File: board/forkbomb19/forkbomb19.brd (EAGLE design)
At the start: 89.2 x 57 mm, 55 parts, among them SW1 SPST_TACT-KMR2, U1 ESP-WROOM-03, X3 POT_GND, X4 POT_3V3, X5 POT_SIG

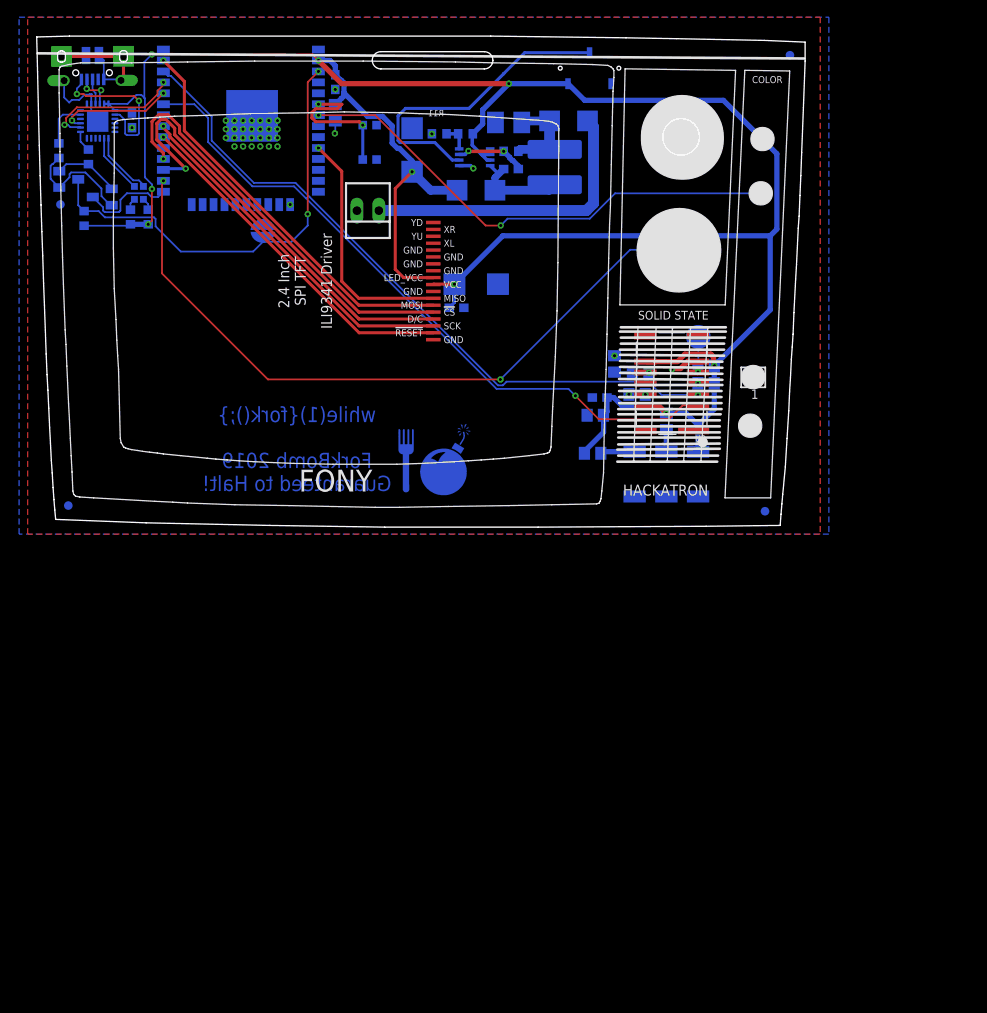
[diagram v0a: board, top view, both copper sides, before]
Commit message: moving to lithium batteries
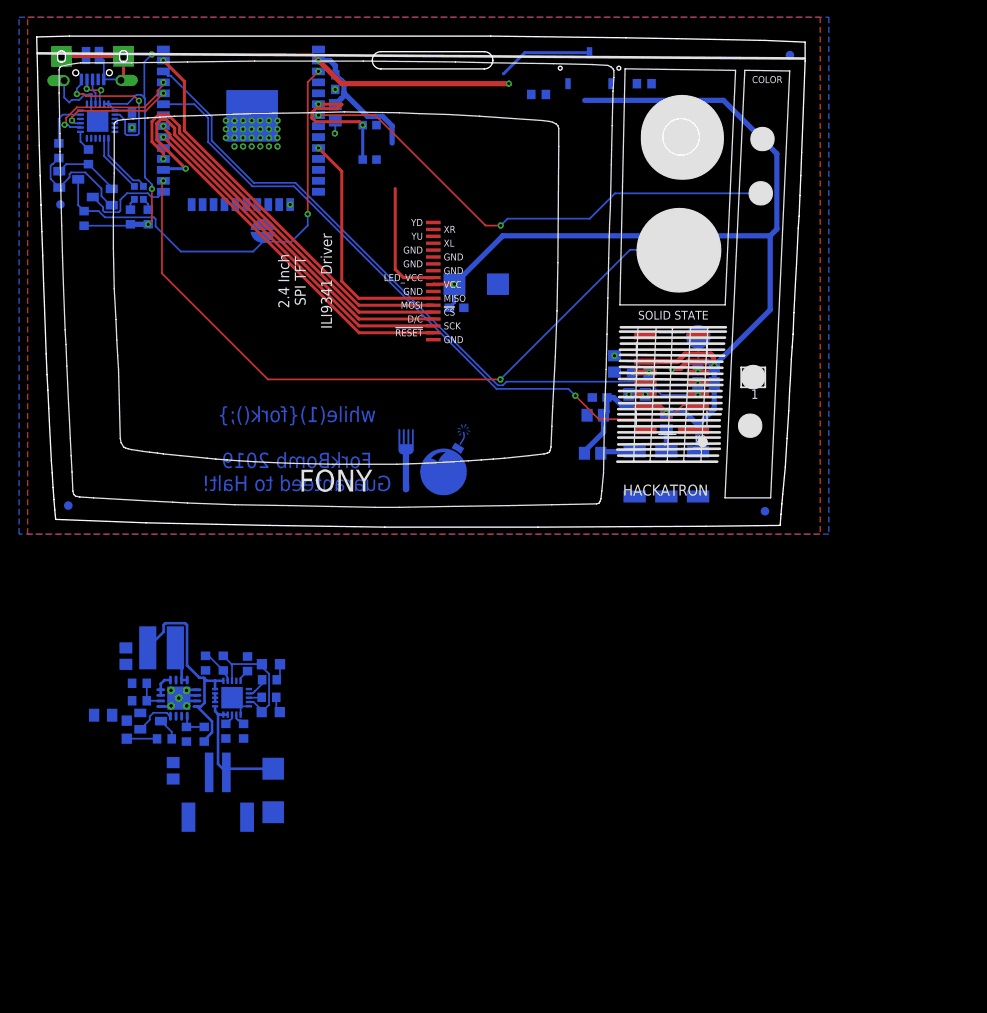
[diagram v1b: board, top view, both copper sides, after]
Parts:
- removed BATT: 22-23-2021, con-molex:22-23-2021
- removed C11: 4.7pF, resistor:C0603
- removed C12: 100uF, resistor:C/6032-28R
- removed D1, D2: MBRS130LT3, diode:SMB
- removed L1: 4.7uH, resistor:POWER-CHOKE_WE-TPC
- removed R10: 165k, resistor:R0603
- removed R11: 100k, resistor:R0603
- removed U$1: LM2623, forkbomb19:SSOP08
- added B1: JST 2-PH, microbuilder:JSTPH2
- added C15: 2.2uF, rcl:C0805
- added C16: 0.1uF, microbuilder:0805_10MGAP
- added C2: 10uF, microbuilder:0805-NO
- added CHRG/LBO: ORANGE, microbuilder:CHIPLED_0805_NOOUTLINE
- added DONE: GREEN, microbuilder:CHIPLED_0805_NOOUTLINE
- added L2: 6.8uH, microbuilder:INDUCTOR_5X5MM_TDK_VLC5045
- added LED1: RED, microbuilder:CHIPLED_0805_NOOUTLINE
- added R18, R21: 200K, rcl:R0603
- added R19: 1.12M, rcl:R0603
- added R20, R27, R28: 1K, rcl:R0603
- added R23: 340K, rcl:R0603
- added R24: 1.87M, rcl:R0603
- added R25: 270K, rcl:R0603
- added R26, R30: 100K, rcl:R0603
- added R29: 1.0K, rcl:R0603
- added T3: MMUN2133LT1G, transistor:SC59-BEC
- added THERM: 15K, rcl:R0603
- added U4: TPS61090RSAR, microbuilder:PVQFN-16
- added U5: MCP73871, microbuilder:QFN20_4MM
- C10: value 22uF -> 100uF; device resistor:T/3528-12R -> rcl:C/6032-28R
- R9: value 150k -> 200k; device resistor:R0603 -> rcl:R0603
- moved C10 82.2 mm to (26.5, -30.8), turned to 90 degrees
- moved R9 17.3 mm to (69.6, 51.3)
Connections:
- removed net N$14: C11.2, R9.1, U$1.3
- removed net N$15: C11.1, D2.A, L1.2, U$1.8
- removed net N$17: U$1.2, U$17.P$2
- removed net N$18: R10.1, R11.2, U$1.4
- removed net N$30: BATT.1, D1.A
- new net ENABLE: U$17.P$2, U4.11
- new net LBO: T3.B, U4.12
- new net N$16: L2.P$2, U4.3, U4.4
- new net N$23: R23.2, R24.1, U4.9
- new net N$24: LED1.A, R20.1
- new net N$25: R19.1, R21.2, U4.14
- new net N$26: R20.2, T3.C
- new net N$28: R25.1, R26.1, U5.P$2
- new net N$29: R28.1, U5.P$7
- new net N$32: R27.1, U5.P$8
- new net N$33: R29.2, U5.P$13
- new net N$34: THERM.2, U5.P$5
- new net N$35: DONE.C, R28.2
- new net N$36: CHRG/LBO.C, R27.2
- new net N$37: R30.2, U5.P$12
- new net N$42: R18.2, U$17.P$3
- new net VBAT: C16.1, C2.1, L2.P$1, R18.1, R24.2, T3.E, U4.8, U5.P$1, U5.P$20
- new net VBUS: CHRG/LBO.A, DONE.A, R25.2, U5.P$17, U5.P$18, U5.P$19, U5.P$3, U5.P$4, U5.P$9
- new net VLIPO: B1.2, C10.+, U5.P$14, U5.P$15, U5.P$16
- net +3V3: now also C15.1, R19.2, U4.1, U4.15, U4.16; no longer C12.+, D2.C, R10.2, U$1.6, U$1.7, U$17.P$3
- net GND: now also B1.1, C15.2, C16.2, C2.2, LED1.C, R21.1, R23.1, R26.2, R29.1, R30.1, R9.2, THERM.1, U4.10, U4.13, U4.5, U4.6, U4.7, U4.P$18, U4.P$19, U4.P$20, U4.P$21, U4.P$22, U4.THERMAL, U5.P$10, U5.P$11, U5.P$21; no longer BATT.2, C12.-, R11.1, U$1.1, U$1.5, U$17.P$1
- net N$13: now also R9.1, U$17.P$1; no longer C10.+, D1.C, L1.1, R9.2
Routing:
- net N$17: track 36.2 -> 0.00 mm
- net N$30: track 35.1 -> 0.00 mm
- net +3V3: track 286.0 -> 252.9 mm, vias 9 -> 8
- net VBAT: track 0.00 -> 26.0 mm
- net VBUS: track 0.00 -> 16.2 mm
- net N$13: track 15.1 -> 0.00 mm
- net VLIPO: track 0.00 -> 15.1 mm
- net N$15: track 12.9 -> 0.00 mm
- net GND: track 31.7 -> 42.7 mm, vias 36 -> 34
- net ENABLE: track 0.00 -> 11.0 mm
- net N$14: track 8.15 -> 0.00 mm, vias 2 -> 0
- net LBO: track 0.00 -> 4.80 mm
- net N$16: track 0.00 -> 4.70 mm
- net N$28: track 0.00 -> 4.17 mm
- net N$25: track 0.00 -> 3.66 mm
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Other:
- board text removed: "+"
- board text removed: "-"

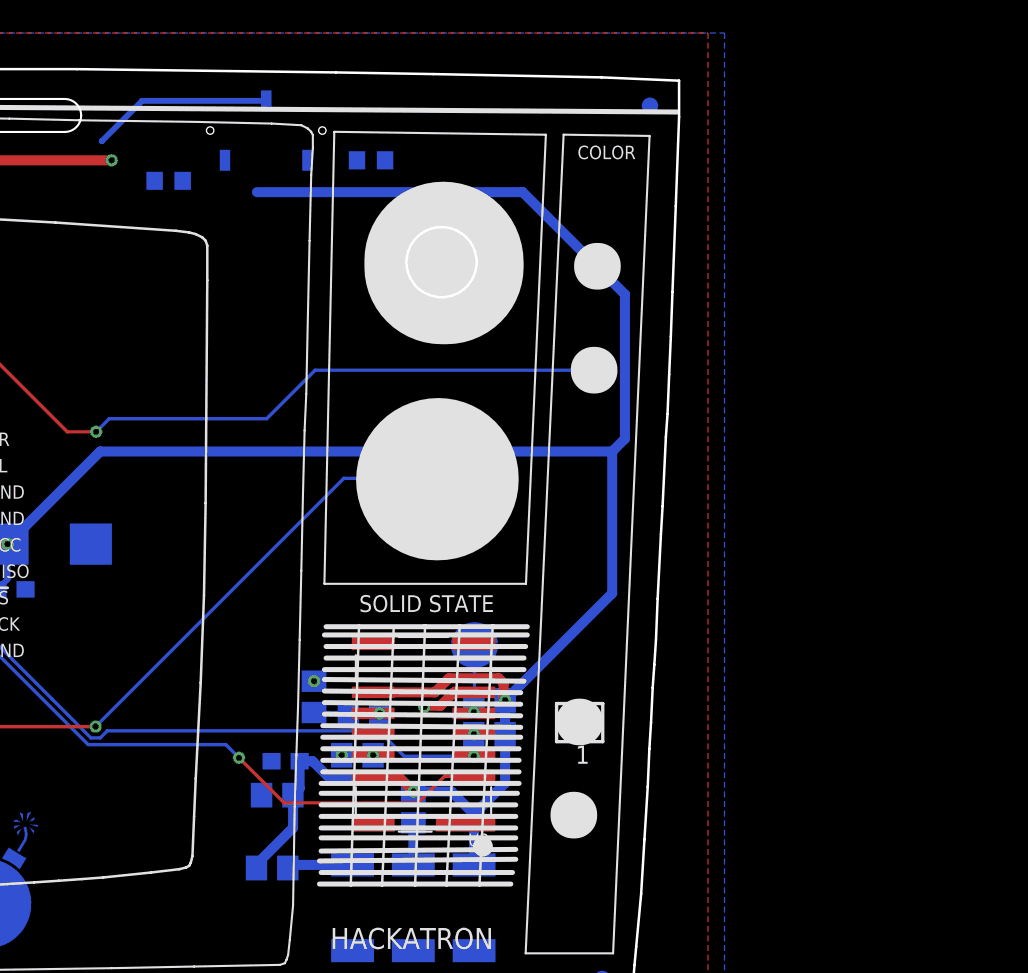
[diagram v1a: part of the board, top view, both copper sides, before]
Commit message: added new thermal sensor part
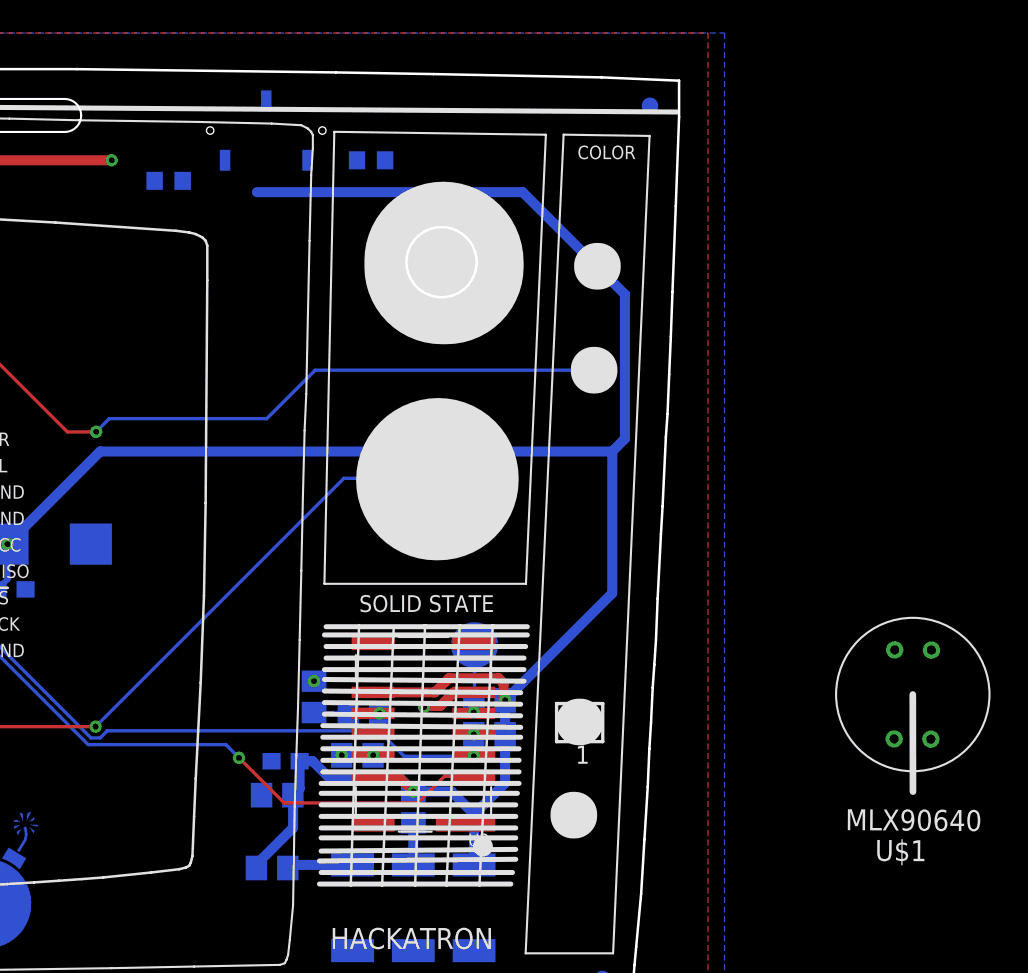
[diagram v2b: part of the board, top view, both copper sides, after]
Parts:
- added U$7: MLX90640, forkbomb19:MLX90640
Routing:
- net ENABLE: track 11.0 -> 0.00 mm
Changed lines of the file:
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@@
 <attribute name="VALUE" x="23.4422" y="-33.7594" size="1.27" layer="28" rot="MR90"/>
 </element>
+<element name="U$7" library="forkbomb19" package="MLX90640" value="MLX90640" x="102.4128" y="18.8976" smashed="yes" rot="R67.2"/>
 </elements>
 <signals>
@@
 <signal name="ENABLE">
 <contactref element="U$17" pad="P$2"/>
-<wire x1="55.6934" y1="54.886" x2="53.2573" y2="52.4499" width="0.3556" layer="16"/>
-<wire x1="53.2573" y1="52.4499" x2="53.2573" y2="52.4420125" width="0.3556" layer="16"/>
-<wire x1="63.2206" y1="54.886" x2="55.6934" y2="54.886" width="0.3556" layer="16"/>
-<wire x1="15.2198" y1="-22.1406" x2="53.2573" y2="52.4499" width="0" layer="19" extent="16-16"/>
 <contactref element="U4" pad="11"/>
+<wire x1="15.2198" y1="-22.1406" x2="63.2206" y2="54.886" width="0" layer="19" extent="16-16"/>
 </signal>
 <signal name="N$25">

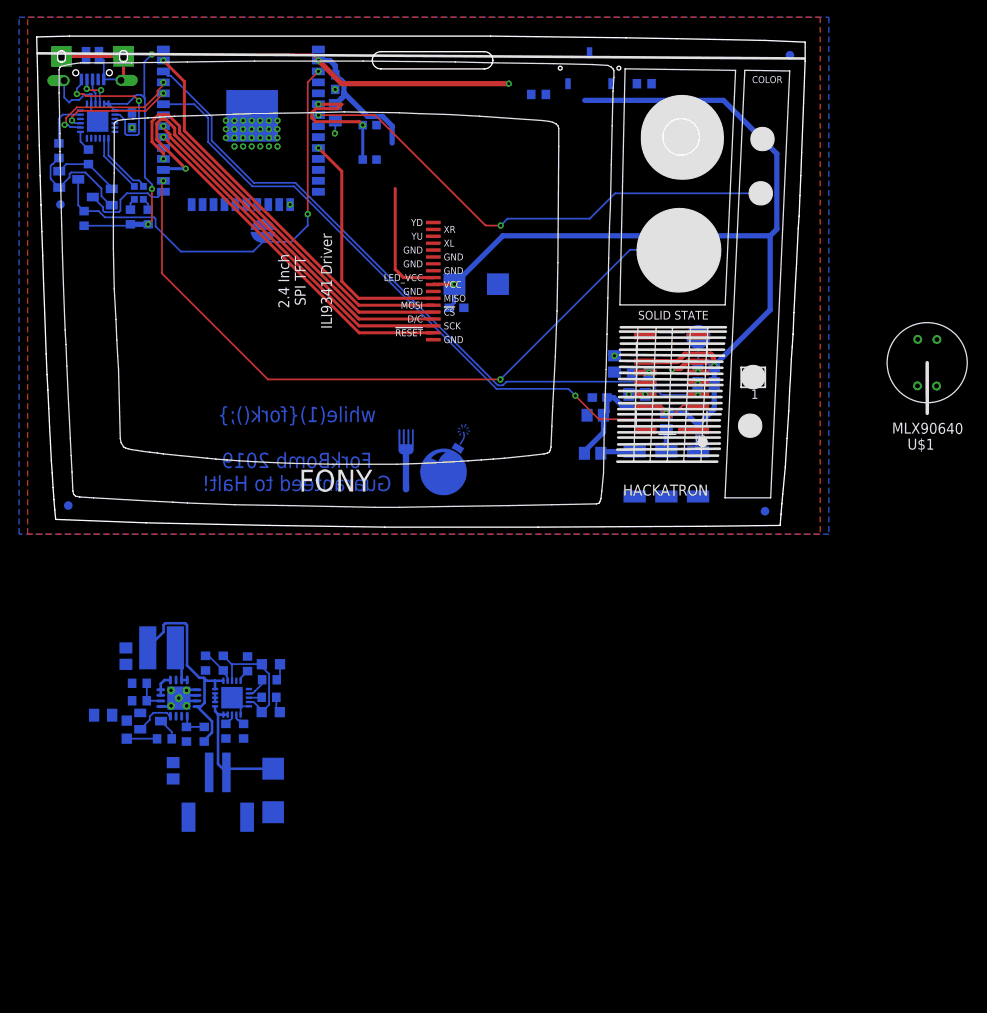
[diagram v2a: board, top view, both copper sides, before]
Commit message: added thermal sensor to the board
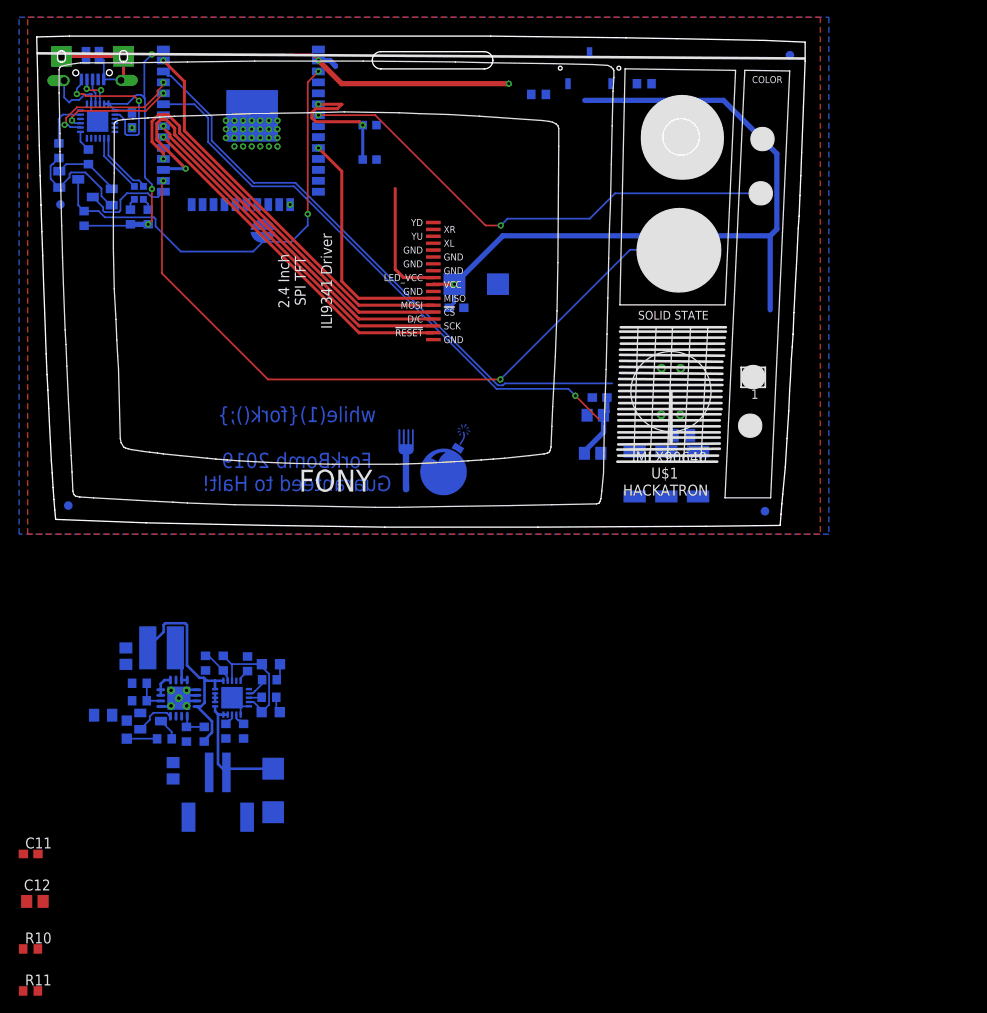
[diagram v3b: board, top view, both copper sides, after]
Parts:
- removed ADDR: (no value), SparkFun-Jumpers:SMT-JUMPER_2_NO_SILK_ROUND
- removed C4: 100nF, resistor:C0603
- removed C5: 10uF, resistor:C0805
- removed C6: 1uF, resistor:C0805
- removed C7: 2.2uF, resistor:C0805
- removed R3: 22, resistor:R0805
- removed R4, R5: 10k, resistor:R0805
- removed U2: (no value), forkbomb19:MICROBUILDER_AMG8833
- added C11: 100nF, resistor:C0603
- added C12: 1uF, resistor:C0805
- added R10, R11: 2.2k, resistor:R0603
- moved U$7 29.9 mm to (72.7, 15.5)
- moved R8 2.37 mm to (73.9, 10.5), turned to 0 degrees
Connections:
- removed net N$10: C6.2, R3.2
- removed net N$11: R4.1, U2.4
- removed net N$7: ADDR.2, R5.1, U2.5
- removed net N$8: C6.1, U2.10
- removed net N$9: C7.1, U2.12
- net +3V3: now also C11.1, C12.1, R10.2, R11.2, U$7.VDD; no longer C4.1, C5.1, R4.2, R5.2, U2.13, U2.9
- net GND: now also C11.2, C12.2, U$7.GND; no longer ADDR.1, C4.2, C5.2, C7.2, R3.1, U2.6
- net I2C_SCL: now also R10.1, U$7.SCL; no longer U2.3
- net I2C_SDA: now also R11.1, U$7.SDA; no longer U2.2
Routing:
- net +3V3: track 252.9 -> 194.1 mm, vias 8 -> 6
- net I2C_SDA: track 79.5 -> 67.3 mm
- net I2C_SCL: track 79.7 -> 68.9 mm, vias 1 -> 0
- net GND: track 42.7 -> 37.9 mm, vias 34 -> 29
- net N$12: track 4.00 -> 0.26 mm
- net N$7: track 2.89 -> 0.00 mm, vias 1 -> 0
- net N$31: track 2.55 -> 0.00 mm
- net N$10: track 2.10 -> 0.00 mm
- net N$8: track 0.40 -> 0.00 mm, vias 1 -> 0
- net N$9: track 0.01 -> 0.00 mm, vias 1 -> 0
- net N$11: vias 1 -> 0

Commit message: TODO: -Make sure all components on the BOM are in stock -Find a potentiometer that fits -Find knobs for the pot -Remake the on/off switch footprint/make sure it's still in stock. Maybe change to side switch? -Make sure the caps are all in the right place and organized like the schematic -Clean up the schematic -Find a proper soft reset switch -Find some male JST connectectors for the batteries -Find some thick double sided tape
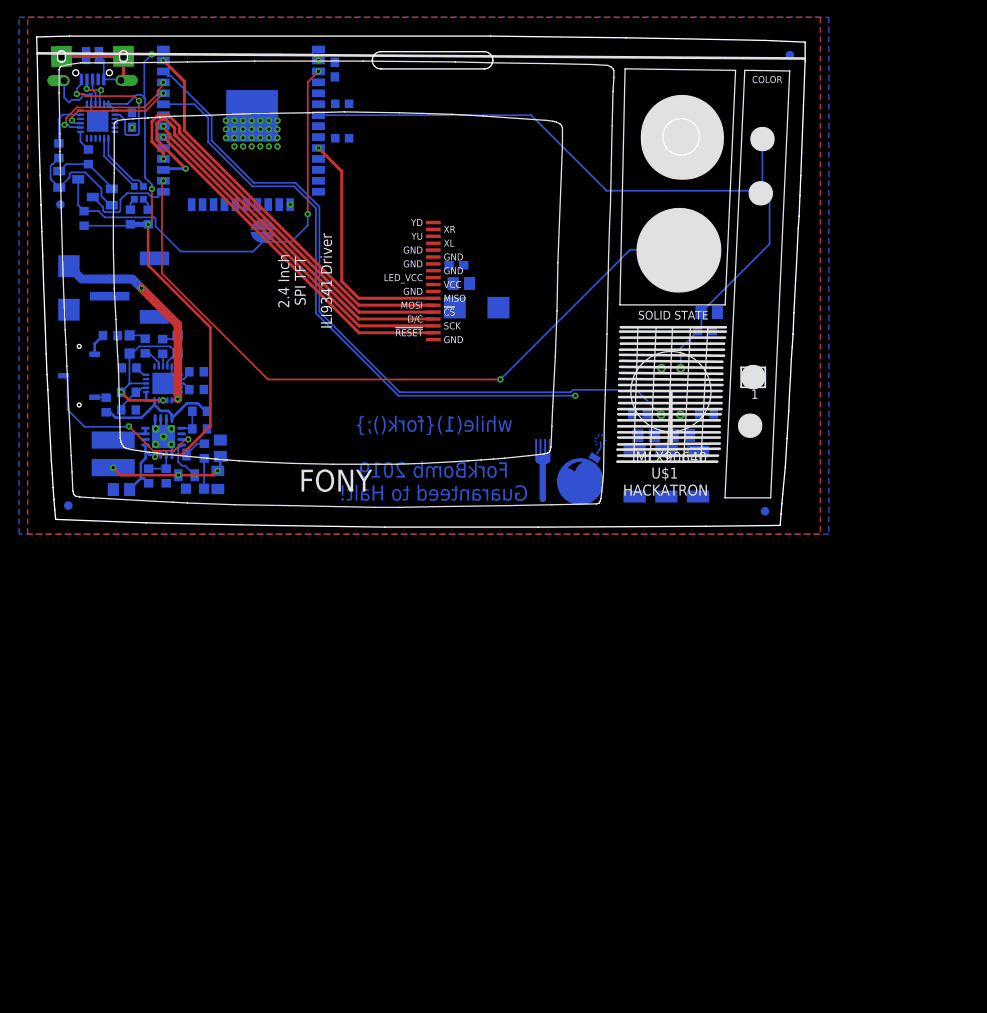
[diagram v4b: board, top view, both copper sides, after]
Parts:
- moved C12 103.9 mm to (77.1, 24.7), flipped to the bottom, turned to 180 degrees
- moved R11 103.2 mm to (76.8, 12.9), flipped to the bottom, turned to 180 degrees
- moved C11 99.0 mm to (76.6, 22.6), flipped to the bottom, turned to 180 degrees
- moved R10 94.1 mm to (69.0, 12.9), flipped to the bottom
- moved U$17 69.2 mm to (3.98, 17.4), turned to 270 degrees
- moved R9 68.5 mm to (7.59, 22.0)
- moved C9 63.1 mm to (10.1, 47.1), turned to 270 degrees
- moved C10 63.0 mm to (2.78, 27.6)
- moved R18 61.8 mm to (7.11, 14.0), turned to 90 degrees
- moved B1 60.6 mm to (11.2, 27.6), turned to 90 degrees
- moved CHRG/LBO 44.0 mm to (15.4, 21.0), turned to 0 degrees
- moved R27 42.6 mm to (13.7, 20.8), turned to 90 degrees
- moved R30 42.1 mm to (17.6, 17.8), turned to 0 degrees
- moved R28 41.3 mm to (11.6, 20.8), turned to 90 degrees
- moved DONE 40.6 mm to (9.83, 21.0), turned to 0 degrees
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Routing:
- net +3V3: track 194.1 -> 131.3 mm, vias 6 -> 5
- net ENABLE: track 0.00 -> 22.1 mm, vias 0 -> 2
- net N$2: track 17.5 -> 0.00 mm, vias 2 -> 0
- net I2C_SCL: track 68.9 -> 83.3 mm
- net VLIPO: track 15.1 -> 26.3 mm, vias 0 -> 2
- net VBAT: track 26.0 -> 31.9 mm, vias 0 -> 3
- net VBUS: track 16.2 -> 21.5 mm, vias 0 -> 2
- net I2C_SDA: track 67.3 -> 70.6 mm
- net N$4: track 58.2 -> 55.1 mm, vias 2 -> 0
- net N$13: track 0.00 -> 2.55 mm
- net N$42: track 0.00 -> 1.35 mm
